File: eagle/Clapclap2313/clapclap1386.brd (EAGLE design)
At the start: 50 x 50 mm, 33 parts, among them IC1 TINY13-20PU, J1 AVR_SPI_PRG_6PTH, K1 4052, M1 Mic, U1 LM386

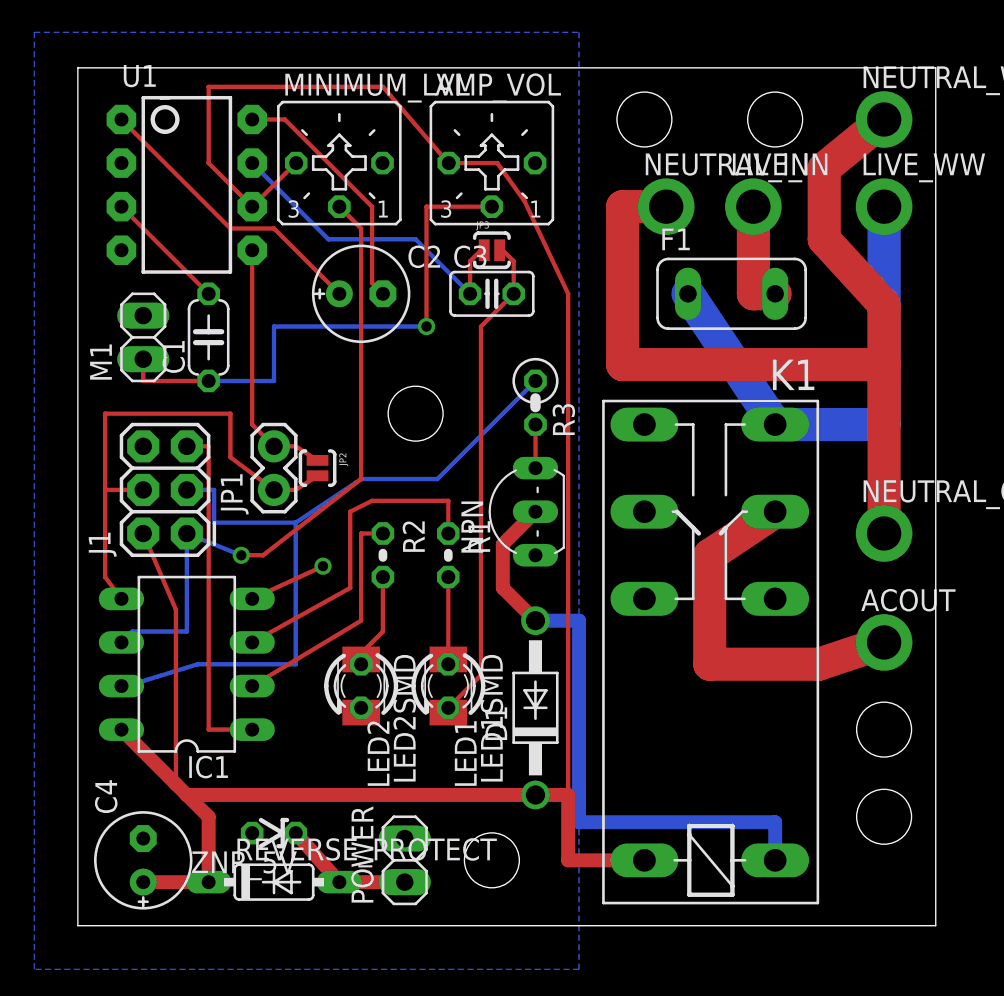
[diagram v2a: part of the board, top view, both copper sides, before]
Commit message: Added a jumper to bypass the input+ of the opamp
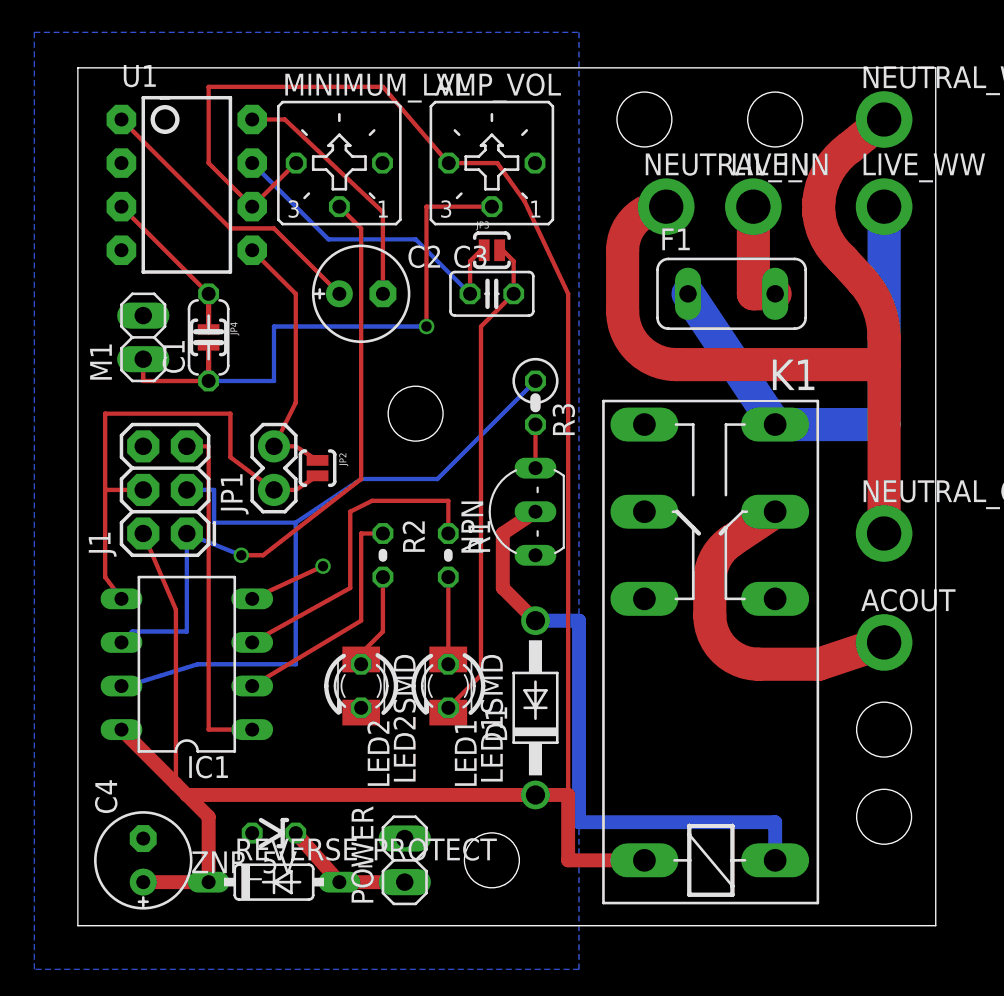
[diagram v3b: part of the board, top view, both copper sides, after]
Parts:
- added JP4: (no value), SparkFun-Passives:SJ_2S-NO
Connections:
- net N$1: now also JP4.1
- net N$3: now also JP4.2
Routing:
- net N$13: track 54.1 -> 50.2 mm
- net N$3: track 31.7 -> 34.0 mm
- net N$1: track 7.18 -> 9.41 mm
- net ACOUT: track 21.3 -> 19.3 mm
- net N$17: track 14.7 -> 15.6 mm
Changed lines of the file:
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@@
 </class>
 </classes>
-<designrules name="default">
+<designrules name="SeeedStudio_DRU_no_angle_20130527">
 <description language="de">&lt;b&gt;EAGLE Design Rules&lt;/b&gt;
 &lt;p&gt;
@@
 necessary adjustments and save your customized
 design rules under a new name.</description>
-<param name="layerSetup" value="(1*16)"/>
-<param name="mtCopper" value="0.035mm 0.035mm 0.035mm 0.035mm 0.035mm 0.035mm 0.035mm 0.035mm 0.035mm 0.035mm 0.035mm 0.035mm 0.035mm 0.035mm 0.035mm 0.035mm"/>
-<param name="mtIsolate" value="1.5mm 0.15mm 0.2mm 0.15mm 0.2mm 0.15mm 0.2mm 0.15mm 0.2mm 0.15mm 0.2mm 0.15mm 0.2mm 0.15mm 0.2mm"/>
-<param name="mdWireWire" value="8mil"/>
-<param name="mdWirePad" value="8mil"/>
-<param name="mdWireVia" value="8mil"/>
-<param name="mdPadPad" value="8mil"/>
-<param name="mdPadVia" value="8mil"/>
-<param name="mdViaVia" value="8mil"/>
-<param name="mdSmdPad" value="8mil"/>
-<param name="mdSmdVia" value="8mil"/>
-<param name="mdSmdSmd" value="8mil"/>
+<description language="zh">&lt;b&gt;Seeed Studio EAGLE Design Rules&lt;/b&gt;
+</description>
+<param name="layerSetup" value="(1*2*15*16)"/>
+<param name="mtCopper" value="0.035mm 0.0175mm 0.035mm 0.035mm 0.035mm 0.035mm 0.035mm 0.035mm 0.035mm 0.035mm 0.035mm 0.035mm 0.035mm 0.035mm 0.0175mm 0.035mm"/>
+<param name="mtIsolate" value="0.2mm 1.1mm 0.2mm 0.15mm 0.2mm 0.15mm 0.2mm 0.15mm 0.2mm 0.15mm 0.2mm 0.15mm 0.2mm 0.15mm 0.2mm"/>
+<param name="mdWireWire" value="6mil"/>
+<param name="mdWirePad" value="6mil"/>
+<param name="mdWireVia" value="6mil"/>
+<param name="mdPadPad" value="6mil"/>
+<param name="mdPadVia" value="6mil"/>
+<param name="mdViaVia" value="6mil"/>
+<param name="mdSmdPad" value="0mil"/>
+<param name="mdSmdVia" value="0mil"/>
+<param name="mdSmdSmd" value="0mil"/>
 <param name="mdViaViaSameLayer" value="8mil"/>
 <param name="mnLayersViaInSmd" value="2"/>
-<param name="mdCopperDimension" value="40mil"/>
-<param name="mdDrill" value="8mil"/>
+<param name="mdCopperDimension" value="10mil"/>
+<param name="mdDrill" value="10mil"/>
 <param name="mdSmdStop" value="0mil"/>
-<param name="msWidth" value="10mil"/>
-<param name="msDrill" value="24mil"/>
-<param name="msMicroVia" value="9.99mm"/>
+<param name="msWidth" value="6mil"/>
+<param name="msDrill" value="12mil"/>
+<param name="msMicroVia" value="12mil"/>
 <param name="msBlindViaRatio" value="0.5"/>
 <param name="rvPadTop" value="0.25"/>
@@
 <param name="rvMicroViaOuter" value="0.25"/>
 <param name="rvMicroViaInner" value="0.25"/>
-<param name="rlMinPadTop" value="10mil"/>
+<param name="rlMinPadTop" value="6mil"/>
 <param name="rlMaxPadTop" value="20mil"/>
-<param name="rlMinPadInner" value="10mil"/>
+<param name="rlMinPadInner" value="6mil"/>
 <param name="rlMaxPadInner" value="20mil"/>
-<param name="rlMinPadBottom" value="10mil"/>
+<param name="rlMinPadBottom" value="6mil"/>
 <param name="rlMaxPadBottom" value="20mil"/>
-<param name="rlMinViaOuter" value="8mil"/>
+<param name="rlMinViaOuter" value="6mil"/>
 <param name="rlMaxViaOuter" value="20mil"/>
-<param name="rlMinViaInner" value="8mil"/>
+<param name="rlMinViaInner" value="6mil"/>
 <param name="rlMaxViaInner" value="20mil"/>
 <param name="rlMinMicroViaOuter" value="4mil"/>
@@
 <param name="psTop" value="-1"/>
 <param name="psBottom" value="-1"/>
-<param name="psFirst" value="-1"/>
+<param name="psFirst" value="0"/>
 <param name="psElongationLong" value="100"/>
 <param name="psElongationOffset" value="100"/>
 <param name="mvStopFrame" value="1"/>
 <param name="mvCreamFrame" value="0"/>
-<param name="mlMinStopFrame" value="4mil"/>
-<param name="mlMaxStopFrame" value="4mil"/>
+<param name="mlMinStopFrame" value="2mil"/>
+<param name="mlMaxStopFrame" value="2mil"/>
 <param name="mlMinCreamFrame" value="0mil"/>
 <param name="mlMaxCreamFrame" value="0mil"/>
-<param name="mlViaStopLimit" value="0mil"/>
+<param name="mlViaStopLimit" value="25mil"/>
 <param name="srRoundness" value="0"/>
 <param name="srMinRoundness" value="0mil"/>
@@
 <param name="checkAngle" value="0"/>
 <param name="checkFont" value="1"/>
-<param name="checkRestrict" value="1"/>
+<param name="checkRestrict" value="0"/>
 <param name="useDiameter" value="13"/>
 <param name="maxErrors" value="50"/>
@@
 <attribute name="OC_FARNELL" value="unknown" x="38.1" y="36.83" size="1.778" layer="27" display="off"/>
 </element>
+<element name="JP4" library="SparkFun-Passives" package="SJ_2S-NO" value="" x="7.62" y="34.29" rot="R270"/>
 </elements>
 <signals>
@@
 <wire x1="7.62" y1="31.75" x2="11.43" y2="31.75" width="0.254" layer="16"/>
 <via x="20.32" y="34.925" extent="1-16" drill="0.6096"/>
+<contactref element="JP4" pad="2"/>
+<wire x1="7.62" y1="31.75" x2="7.62" y2="33.9725" width="0.3048" layer="1"/>
+<wire x1="7.62" y1="33.9725" x2="7.62" y2="33.84" width="0" layer="19" extent="1-1"/>
 </signal>
 <signal name="N$10">
@@
 <contactref element="NPN" pad="C"/>
 <contactref element="D1" pad="A"/>
-<wire x1="24.765" y1="22.225" x2="26.67" y2="24.13" width="0.8128" layer="1"/>
-<wire x1="24.765" y1="19.685" x2="24.765" y2="22.225" width="0.8128" layer="1"/>
+<wire x1="24.765" y1="22.86" x2="26.67" y2="24.13" width="0.8128" layer="1"/>
+<wire x1="24.765" y1="19.685" x2="24.765" y2="22.86" width="0.8128" layer="1"/>
 <wire x1="26.67" y1="17.78" x2="24.765" y2="19.685" width="0.8128" layer="1"/>
 <wire x1="40.64" y1="6.0325" x2="40.64" y2="3.81" width="0.8128" layer="16"/>
@@
 <contactref element="K1" pad="P1"/>
 <contactref element="ACOUT" pad="1"/>
-<wire x1="36.83" y1="15.24" x2="36.83" y2="21.59" width="1.9304" layer="1"/>
-<wire x1="36.83" y1="21.59" x2="40.64" y2="24.13" width="1.9304" layer="1"/>
+<wire x1="43.18" y1="15.24" x2="39.66980625" y2="15.24" width="1.9304" layer="1"/>
+<wire x1="39.66980625" y1="15.24" x2="36.83" y2="18.07980625" width="1.9304" layer="1" curve="-90"/>
+<wire x1="36.83" y1="18.07980625" x2="36.83" y2="20.07018125" width="1.9304" layer="1"/>
+<wire x1="36.83" y1="20.07018125" x2="38.094565625" y2="22.43304375" width="1.9304" layer="1" curve="-56.30995"/>
+<wire x1="38.094565625" y1="22.43304375" x2="40.64" y2="24.13" width="1.9304" layer="1"/>
 <wire x1="46.99" y1="16.51" x2="43.18" y2="15.24" width="1.9304" layer="1"/>
-<wire x1="43.18" y1="15.24" x2="36.83" y2="15.24" width="1.9304" layer="1"/>
 </signal>
 <signal name="N$13">
@@
 <contactref element="NEUTRAL_OUT" pad="1"/>
 <contactref element="NEUTRAL_WW" pad="1"/>
-<wire x1="43.4975" y1="40.005" x2="46.99" y2="36.195" width="1.9304" layer="1"/>
-<wire x1="46.99" y1="36.195" x2="46.99" y2="32.7025" width="1.9304" layer="1"/>
+<wire x1="43.18" y1="42.1707875" x2="43.18" y2="41.552478125" width="1.9304" layer="1"/>
+<wire x1="43.18" y1="41.552478125" x2="44.54316875" y2="38.864271875" width="1.9304" layer="1" curve="42.510397"/>
+<wire x1="44.54316875" y1="38.864271875" x2="45.686415625" y2="37.61709375" width="1.9304" layer="1"/>
+<wire x1="45.686415625" y1="37.61709375" x2="46.99" y2="34.265834375" width="1.9304" layer="1" curve="-42.510427"/>
+<wire x1="46.99" y1="34.265834375" x2="46.99" y2="32.7025" width="1.9304" layer="1"/>
 <wire x1="46.99" y1="32.7025" x2="46.99" y2="22.86" width="1.9304" layer="1"/>
-<wire x1="43.4975" y1="44.1325" x2="43.4975" y2="40.005" width="1.9304" layer="1"/>
-<wire x1="46.99" y1="46.99" x2="43.4975" y2="44.1325" width="1.9304" layer="1"/>
-<wire x1="34.29" y1="41.91" x2="31.75" y2="41.91" width="1.9304" layer="1"/>
-<wire x1="31.75" y1="41.91" x2="31.75" y2="32.7025" width="1.9304" layer="1"/>
-<wire x1="31.75" y1="32.7025" x2="46.99" y2="32.7025" width="1.9304" layer="1"/>
+<wire x1="46.99" y1="46.99" x2="45.01578125" y2="45.37473125" width="1.9304" layer="1"/>
+<wire x1="45.01578125" y1="45.37473125" x2="43.18" y2="42.1707875" width="1.9304" layer="1" curve="50.710584"/>
+<wire x1="34.29" y1="41.91" x2="31.75" y2="39.37" width="1.9304" layer="1" curve="90"/>
+<wire x1="31.75" y1="39.37" x2="31.75" y2="35.829509375" width="1.9304" layer="1"/>
+<wire x1="31.75" y1="35.829509375" x2="34.877009375" y2="32.7025" width="1.9304" layer="1" curve="90"/>
+<wire x1="34.877009375" y1="32.7025" x2="46.99" y2="32.7025" width="1.9304" layer="1"/>
 </signal>
 <signal name="N$1">
@@
 <contactref element="U1" pad="3"/>
 <wire x1="2.54" y1="41.91" x2="7.62" y2="36.83" width="0.254" layer="1"/>
+<contactref element="JP4" pad="1"/>
+<wire x1="7.62" y1="36.83" x2="7.62" y2="34.6075" width="0.3048" layer="1"/>
+<wire x1="7.62" y1="34.6075" x2="7.62" y2="34.74" width="0" layer="19" extent="1-1"/>
 </signal>
 <signal name="N$14">
 <contactref element="U1" pad="8"/>
 <contactref element="C2" pad="-"/>
-<wire x1="17.145" y1="37.465" x2="17.78" y2="36.83" width="0.254" layer="1"/>
-<wire x1="17.145" y1="41.91" x2="17.145" y2="37.465" width="0.254" layer="1"/>
-<wire x1="12.065" y1="46.99" x2="17.145" y2="41.91" width="0.254" layer="1"/>
+<wire x1="17.78" y1="41.5925" x2="17.78" y2="36.83" width="0.254" layer="1"/>
+<wire x1="12.065" y1="46.99" x2="17.78" y2="41.5925" width="0.254" layer="1"/>
 <wire x1="10.16" y1="46.99" x2="12.065" y2="46.99" width="0.254" layer="1"/>
 </signal>
@@
 <wire x1="12.7" y1="27.94" x2="13.97" y2="27.12" width="0.254" layer="1"/>
 <wire x1="11.43" y1="27.94" x2="12.7" y2="27.94" width="0.254" layer="1"/>
-<wire x1="11.43" y1="27.94" x2="10.16" y2="29.21" width="0.254" layer="1"/>
-<wire x1="10.16" y1="29.21" x2="10.16" y2="39.37" width="0.254" layer="1"/>
+<wire x1="11.43" y1="27.94" x2="12.7" y2="30.48" width="0.254" layer="1"/>
+<wire x1="12.7" y1="30.48" x2="12.7" y2="36.83" width="0.254" layer="1"/>
+<wire x1="12.7" y1="36.83" x2="10.16" y2="39.37" width="0.254" layer="1"/>
 </signal>
 <signal name="N$5">

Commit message: v1.0 sent to production in HK.
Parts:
- removed JP4: (no value), SparkFun-Passives:SJ_2S-NO
- added JP5, JP7, JP8: (no value), SparkFun-Passives:SJ_2S-NO
- added JP6, JP9: (no value), SparkFun-Connectors:1X02
- C2: value 10uF -> >=1uF; device resistor:E2,5-6E -> resistor:C050-024X044
- moved C2 15.3 mm to (6.35, 48.3)
- moved AMP_VOL 8.89 mm to (15.2, 44.5)
- moved MINIMUM_LVL 8.89 mm to (24.1, 44.5)
- moved C1 2.54 mm to (10.2, 34.3), turned to 180 degrees
- moved LED1SMD 2.29 mm to (19.7, 12.7)
- moved C3 1.91 mm to (26.0, 36.8)
- moved JP3 1.91 mm to (26.0, 39.4)
- moved U1 1.91 mm to (6.35, 41.3)
- moved LED2SMD 1.80 mm to (15.2, 12.7)
- moved LED2 1.42 mm to (17.1, 12.7)
- moved LED1 1.27 mm to (21.6, 12.7)
- moved IC1 1.27 mm to (6.35, 14.0)
- moved R1 1.27 mm to (21.6, 20.3)
- moved R2 1.27 mm to (17.8, 20.3)
- moved M1 1.27 mm to (3.81, 33.0)
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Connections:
- removed net N$2: IC1.7, J1.3, R3.1
- new net N$21: JP6.1, JP7.2, MINIMUM_LVL.S
- new net N$23: IC1.7, J1.3, JP8.1, JP9.2
- new net N$24: JP8.2, JP9.1, R3.1
- net N$1: no longer JP4.1
- net N$12: now also JP6.2, JP7.1; no longer MINIMUM_LVL.S
- net N$14: now also C2.2, JP5.2; no longer C2.-
- net N$3: no longer JP4.2
- net N$5: now also C2.1, JP5.1; no longer C2.+
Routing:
- net N$23: track 0.00 -> 55.4 mm
- net N$2: track 44.3 -> 0.00 mm
- net GND: track 33.8 -> 12.0 mm
- net N$3: track 34.0 -> 19.9 mm
- net N$21: track 0.00 -> 12.5 mm
- net N$5: track 16.9 -> 5.38 mm
- net N$14: track 14.5 -> 5.70 mm
- net N$24: track 0.00 -> 8.36 mm
- net N$12: track 38.1 -> 33.6 mm
- net N$15: track 18.8 -> 21.4 mm
- net N$6: track 18.8 -> 16.7 mm
- net N$4: track 13.8 -> 15.8 mm
- net N$1: track 9.41 -> 7.65 mm
- net N$7: track 5.36 -> 7.01 mm
- net N$17: track 15.6 -> 17.0 mm
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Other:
- board text added: "+MIC-"
- board text added: "-"
- board text added: "-ZNR+"
- board text added: "5v VCC"
- board text added: "942H-2C-5DS"
- board text added: "A/C IN"
- board text added: "A/C OUT"
- board text added: "A/C WWART"
- board text added: "AMP_VOL"
- board text added: "Attiny13"
- board text added: "B"
- board text added: "C"
- board text added: "C1"
- board text added: "C2"
- board text added: "C3"
- board text added: "C4"
- board text added: "Clap clap ! [1386]"
- board text added: "Clapclap 1386 v1.0 Feb2014"
- board text added: "D1"
- board text added: "E"
- board text added: "Fuse/PTC"
- board text added: "GND"
- board text added: "J1"
- board text added: "J2"
- board text added: "J3"
- board text added: "L"
- board text added: "LED CLAP"
- board text added: "LED SWTCH"
- board text added: "LM386"
- board text added: "MIN_LVL"
- board text added: "N"
- board text added: "NPN"
- board text added: "R1"
- board text added: "R2"
- board text added: "R3"
- board text added: "RVRS_PROTECT"
- board text added: "Relay"
- board text added: "http://kalshagar.wikispaces.com/Clapclap+1386"
